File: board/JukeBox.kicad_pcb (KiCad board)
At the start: 2 copper layers, 78.5 x 80 mm, 57 parts, among them J1 USB_C_Receptacle_USB2.0, J2 Conn_01x02, J3 Conn_01x04, J4 Conn_01x03, J5 Conn_01x08, SW1 SW_SPST, SW10 SW_SPST, SW11 SW_SPST, SW12 SW_SPST, SW2 SW_SPST, SW3 SW_SPST, SW4 SW_SPST, SW5 SW_SPST, SW6 SW_SPST, SW7 SW_SPST, SW8 SW_SPST, SW9 SW_SPST, U1 ATmega8U2-A, Y1 16MHz

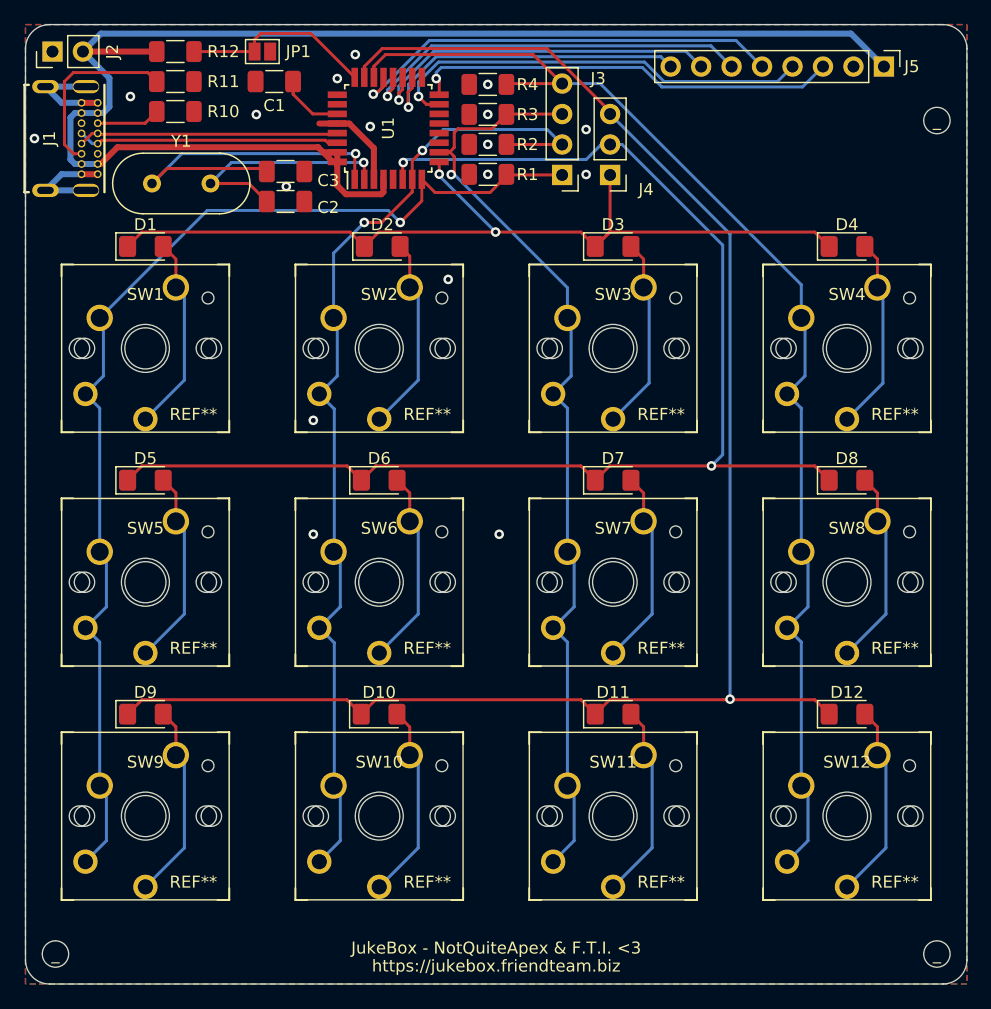
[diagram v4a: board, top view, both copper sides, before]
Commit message: fix resistors for usb in pcb
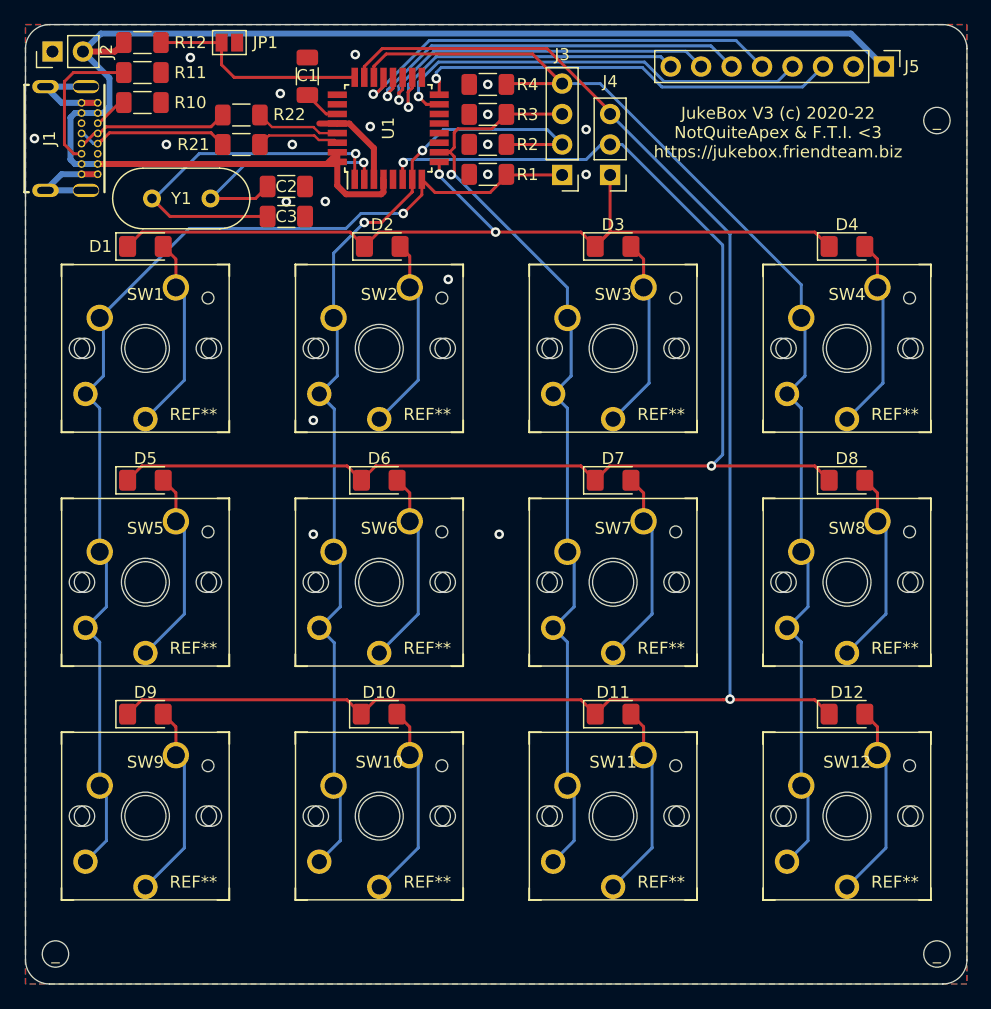
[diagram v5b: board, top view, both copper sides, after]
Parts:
- added R21: 22, Resistor_SMD:R_1206_3216Metric_Pad1.30x1.75mm_HandSolder, F.Cu at (125.0, 45.0)
- added R22: 22, Resistor_SMD:R_1206_3216Metric_Pad1.30x1.75mm_HandSolder, F.Cu at (125.0, 42.5)
- moved C3 3.75 mm to (128.8, 51.0)
- moved JP1 2.85 mm to (124.0, 36.5)
- moved R10 2.85 mm to (116.8, 41.5)
- moved R11 2.85 mm to (116.8, 39.0)
- moved R12 2.85 mm to (116.8, 36.5)
- moved C1 2.78 mm to (130.5, 39.3), turned to -90 degrees
- moved C2 1.25 mm to (128.8, 48.5)
- moved Y1 1.25 mm to (117.5, 49.5)
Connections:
- U1 pad 29: /D+ -> /D1+
- U1 pad 30: /D- -> /D1-
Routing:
- net /D+: track 21.8 -> 12.9 mm
- net /D-: track 21.1 -> 13.0 mm
- net /D1+: track 0.00 -> 7.08 mm
- net /D1-: track 0.00 -> 7.01 mm
- net Net-(J1-PadB5): track 15.5 -> 12.5 mm
- net +5V: track 120.1 -> 117.2 mm
- net Net-(J1-PadA5): track 5.33 -> 2.89 mm
- net Net-(JP1-Pad2): track 16.1 -> 18.4 mm
- net Net-(C1-Pad2): track 5.43 -> 3.15 mm
- net COL_1: track 95.4 -> 94.3 mm
- net Net-(C3-Pad2): track 30.4 -> 31.1 mm
- net GND: vias 17 -> 19
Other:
- board text added: "JukeBox V3 (c) 2020-22 NotQuiteApex & F.T.I. <3 https://jukebox.friendteam.biz"
- board text removed: "JukeBox - NotQuiteApex & F.T.I. <3"
- board text removed: "https://jukebox.friendteam.biz"

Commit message: import rp2040 minimal kicad project
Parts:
- removed D1, D10, D11, D12, D2, D3, D4, D5, D6, D7, D8, D9: DIODE, Diode_SMD:D_1206_3216Metric_Pad1.42x1.75mm_HandSolder
- removed J5: Conn_01x08, Connector_PinHeader_2.54mm:PinHeader_1x08_P2.54mm_Vertical
- removed JP1: , Jumper:SolderJumper-2_P1.3mm_Open_Pad1.0x1.5mm
- removed R10, R11: 5.11k, Resistor_SMD:R_1206_3216Metric_Pad1.30x1.75mm_HandSolder
- removed R12: 10K, Resistor_SMD:R_1206_3216Metric_Pad1.30x1.75mm_HandSolder
- removed R21, R22: 22, Resistor_SMD:R_1206_3216Metric_Pad1.30x1.75mm_HandSolder
- removed REF** (x12): SW_Cherry_MX_1.00u_PCB, Button_Switch_Keyboard:SW_Cherry_MX_1.00u_PCB
- removed SW1, SW10, SW11, SW12, SW2, SW3, SW4, SW5, SW6, SW7, SW8, SW9: SW_SPST, jukebox-footprints:Kailh_PG1350
- removed _ (x3): MountingHole_2.2mm_M2, MountingHole:MountingHole_2.2mm_M2
- added C10: 1u, Capacitor_SMD:C_0402_1005Metric, F.Cu at (104.0, 93.5)
- added C11: 100n, Capacitor_SMD:C_0402_1005Metric, F.Cu at (93.5, 97.0)
- added C12: 100n, Capacitor_SMD:C_0402_1005Metric, F.Cu at (106.5, 101.2)
- added C13: 100n, Capacitor_SMD:C_0402_1005Metric, F.Cu at (93.5, 101.2)
- added C14: 100n, Capacitor_SMD:C_0402_1005Metric, F.Cu at (100.4, 106.5)
- added C15: 100n, Capacitor_SMD:C_0402_1005Metric, F.Cu at (106.5, 96.0)
- added C16: 100n, Capacitor_SMD:C_0402_1005Metric, F.Cu at (106.5, 94.6)
- added C17: 10u, Capacitor_SMD:C_0805_2012Metric, F.Cu at (85.1, 78.0)
- added C4: 10u, Capacitor_SMD:C_0805_2012Metric, F.Cu at (109.0, 89.0)
- added C5: 100n, Capacitor_SMD:C_0402_1005Metric, F.Cu at (96.2, 82.8)
- added C6: 100n, Capacitor_SMD:C_0402_1005Metric, F.Cu at (99.0, 92.5)
- added C7: 100n, Capacitor_SMD:C_0402_1005Metric, F.Cu at (101.5, 106.5)
- added C8: 1u, Capacitor_SMD:C_0402_1005Metric, F.Cu at (103.0, 93.5)
- added C9: 100n, Capacitor_SMD:C_0402_1005Metric, F.Cu at (100.0, 92.5)
- added H1: MountingHole, MountingHole:MountingHole_2.7mm_M2.5, F.Cu at (86.0, 74.0)
- added H2: MountingHole, MountingHole:MountingHole_2.7mm_M2.5, F.Cu at (114.0, 74.0)
- added H3: MountingHole, MountingHole:MountingHole_2.7mm_M2.5, F.Cu at (114.0, 117.2)
- added H4: MountingHole, MountingHole:MountingHole_2.7mm_M2.5, F.Cu at (86.0, 117.2)
- added R5: 1k, Capacitor_SMD:C_0402_1005Metric, F.Cu at (98.7, 107.1)
- added U2: W25Q128JVS, Package_SO:SOIC-8_5.23x5.23mm_P1.27mm, F.Cu at (93.0, 87.3)
- added U3: RP2040, RP2040_minimal:RP2040-QFN-56, F.Cu at (100.0, 100.0)
- C1: value 1uF -> 10u; footprint Capacitor_SMD:C_1206_3216Metric_Pad1.33x1.80mm_HandSolder -> Capacitor_SMD:C_0805_2012Metric
- C2, C3: value 18pF -> 27p; footprint Capacitor_SMD:C_1206_3216Metric_Pad1.33x1.80mm_HandSolder -> Capacitor_SMD:C_0402_1005Metric
- J1: value USB_C_Receptacle_USB2.0 -> USB_B_Micro; footprint jukebox-footprints:GCT_USB4085-GF-A_REVA4 -> RP2040_minimal:USB_Micro-B_Amphenol_10103594-0001LF_Horizontal_modified
- J3: value Conn_01x04 -> Conn_02x18_Odd_Even; footprint Connector_PinHeader_2.54mm:PinHeader_1x04_P2.54mm_Vertical -> Connector_PinHeader_2.54mm:PinHeader_2x18_P2.54mm_Vertical
- J4: value Conn_01x03 -> Conn_02x18_Odd_Even; footprint Connector_PinHeader_2.54mm:PinHeader_1x03_P2.54mm_Vertical -> Connector_PinHeader_2.54mm:PinHeader_2x18_P2.54mm_Vertical
- R1: value 10k -> 1k; footprint Resistor_SMD:R_1206_3216Metric_Pad1.30x1.75mm_HandSolder -> Capacitor_SMD:C_0402_1005Metric
- R2: value 10k -> DNF; footprint Resistor_SMD:R_1206_3216Metric_Pad1.30x1.75mm_HandSolder -> Capacitor_SMD:C_0402_1005Metric
- R3, R4: value 10k -> 27; footprint Resistor_SMD:R_1206_3216Metric_Pad1.30x1.75mm_HandSolder -> Capacitor_SMD:C_0402_1005Metric
- U1: value ATmega8U2-A -> NCP1117-3.3_SOT223; footprint Package_QFP:TQFP-32_7x7mm_P0.8mm -> Package_TO_SOT_SMD:SOT-223-3_TabPin2
- Y1: value 16MHz -> ABLS-12.000MHZ-B4-T; footprint Crystal:Crystal_HC49-4H_Vertical -> RP2040_minimal:Crystal_SMD_HC49-US
- moved J3 80.4 mm to (75.9, 74.0), turned to 0 degrees
- moved R4 69.0 mm to (102.0, 93.5), turned to -90 degrees
- moved C2 68.6 mm to (96.5, 109.0)
- moved R3 67.7 mm to (101.0, 93.5), turned to -90 degrees
- moved R2 67.3 mm to (89.5, 82.3), turned to -90 degrees
- moved Y1 66.6 mm to (97.8, 113.1)
- moved C3 65.0 mm to (99.5, 109.0), turned to 0 degrees
- moved R1 64.7 mm to (91.0, 82.3), turned to 90 degrees
- moved U1 48.9 mm to (108.0, 82.8), turned to -90 degrees
- moved C1 43.5 mm to (107.9, 76.5), turned to 0 degrees
- moved J2 43.3 mm to (91.1, 76.5), turned to 180 degrees
- moved J4 43.2 mm to (121.6, 74.0), turned to 0 degrees
- moved J1 28.7 mm to (100.0, 71.7), turned to 180 degrees
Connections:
- C1 pad 1: GND -> VBUS
- C1 pad 2: Net-(C1-Pad2) -> GND
- C2 pad 1: GND -> /XIN
- C2 pad 2: Net-(C2-Pad2) -> GND
- C3 pad 1: GND -> Net-(C3-Pad1)
- C3 pad 2: Net-(C3-Pad2) -> GND
- J2 pad 1: GND -> /~{USB_BOOT}
- J2 pad 2: +5V -> GND
- J3 pad 1: COL_1 -> GND
- J3 pad 2: COL_2 -> +3V3
- J3 pad 3: COL_3 -> GND
- J3 pad 4: COL_4 -> /GPIO0
- J4 pad 1: ROW_1 -> /GPIO29_ADC3
- J4 pad 2: ROW_2 -> GND
- J4 pad 3: ROW_3 -> /GPIO28_ADC2
- R1 pad 1: GND -> /QSPI_SS
- R1 pad 2: COL_1 -> /~{USB_BOOT}
- R2 pad 1: GND -> +3V3
- R2 pad 2: COL_2 -> /QSPI_SS
- R3 pad 1: GND -> /USB_D+
- R3 pad 2: COL_3 -> Net-(R3-Pad2)
- R4 pad 1: GND -> /USB_D-
- R4 pad 2: COL_4 -> Net-(R4-Pad2)
- U1 pad 1: Net-(C3-Pad2) -> GND
- U1 pad 2: Net-(C2-Pad2) -> +3V3
- U1 pad 3: GND -> VBUS
- Y1 pad 1: Net-(C3-Pad2) -> /XIN
- Y1 pad 2: Net-(C2-Pad2) -> Net-(C3-Pad1)
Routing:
- net ROW_3: track 138.8 -> 0.00 mm, vias 1 -> 0
- net +5V: track 117.2 -> 0.00 mm
- net ROW_2: track 112.4 -> 0.00 mm, vias 2 -> 0
- net COL_4: track 101.4 -> 0.00 mm
- net COL_1: track 94.3 -> 0.00 mm, vias 1 -> 0
- net COL_2: track 84.4 -> 0.00 mm, vias 2 -> 0
- net COL_3: track 80.4 -> 0.00 mm, vias 1 -> 0
- net ROW_1: track 75.8 -> 0.00 mm, vias 2 -> 0
- net +3V3: track 0.00 -> 45.2 mm, vias 0 -> 2
- net CS: track 37.0 -> 0.00 mm, vias 1 -> 0
- net CLK: track 36.3 -> 0.00 mm, vias 1 -> 0
- net DIN: track 35.8 -> 0.00 mm, vias 1 -> 0
- net DC: track 33.2 -> 0.00 mm, vias 1 -> 0
- net /GPIO29_ADC3: track 0.00 -> 33.2 mm
- net /GPIO0: track 0.00 -> 31.8 mm
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- added copper zone on F.Cu, net +1V1
- added copper zone on F.Cu, net +3V3
- added copper zone on F.Cu, net VBUS
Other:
- board size 78.5 x 80 mm -> 52 x 51 mm
- rule pad_to_mask_clearance: 0 -> 0.051
- board text added: "3V3"
- board text added: "GND"
- board text added: "GP0"
- board text added: "GP1"
- board text added: "GP10"
- board text added: "GP11"
- board text added: "GP12"
- board text added: "GP13"
- board text added: "GP14"
- board text added: "GP15"
- board text added: "GP16"
- board text added: "GP17"
- board text added: "GP18"
- board text added: "GP19"
- board text added: "GP2"
- board text added: "GP20"
- board text added: "GP21"
- board text added: "GP22"
- board text added: "GP23"
- board text added: "GP24"
- board text added: "GP25"
- board text added: "GP26"
- board text added: "GP27"
- board text added: "GP28"
- board text added: "GP29"
- board text added: "GP3"
- board text added: "GP4"
- board text added: "GP5"
- board text added: "GP6"
- board text added: "GP7"
- board text added: "GP8"
- board text added: "GP9"
- board text added: "Minimal Design Example REV1"
- board text added: "Outer Row GND"
- board text added: "RUN"
- board text added: "Raspberry Pi RP2040"
- board text added: "SWCLK"
- board text added: "SWD"
- board text added: "USB_BOOT"
- board text removed: "JukeBox V3 (c) 2020-22 NotQuiteApex & F.T.I. <3 https://jukebox.friendteam.biz"

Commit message: first pass over pcb
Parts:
- removed C11, C12, C13, C14, C15, C16, C9: 100n, Capacitor_SMD:C_0402_1005Metric
- removed C17: 10u, Capacitor_SMD:C_0805_2012Metric
- removed J4: Conn_02x18_Odd_Even, Connector_PinHeader_2.54mm:PinHeader_2x18_P2.54mm_Vertical
- added D1: DIODE, Diode_SMD:D_1206_3216Metric_Pad1.42x1.75mm_HandSolder, B.Cu at (61.1, 72.5)
- added D10: DIODE, Diode_SMD:D_1206_3216Metric_Pad1.42x1.75mm_HandSolder, B.Cu at (80.6, 111.5)
- added D11: DIODE, Diode_SMD:D_1206_3216Metric_Pad1.42x1.75mm_HandSolder, B.Cu at (100.1, 111.5)
- added D12: DIODE, Diode_SMD:D_1206_3216Metric_Pad1.42x1.75mm_HandSolder, B.Cu at (119.6, 111.5)
- added D13: WS2812B, LED_SMD:LED_WS2812B_PLCC4_5.0x5.0mm_P3.2mm, F.Cu at (61.1, 70.0)
- added D14: WS2812B, LED_SMD:LED_WS2812B_PLCC4_5.0x5.0mm_P3.2mm, F.Cu at (80.6, 70.0)
- added D15: WS2812B, LED_SMD:LED_WS2812B_PLCC4_5.0x5.0mm_P3.2mm, F.Cu at (100.1, 70.0)
- added D16: WS2812B, LED_SMD:LED_WS2812B_PLCC4_5.0x5.0mm_P3.2mm, F.Cu at (119.6, 70.0)
- added D17: WS2812B, LED_SMD:LED_WS2812B_PLCC4_5.0x5.0mm_P3.2mm, F.Cu at (61.1, 89.5)
- added D18: WS2812B, LED_SMD:LED_WS2812B_PLCC4_5.0x5.0mm_P3.2mm, F.Cu at (80.6, 89.5)
- added D19: WS2812B, LED_SMD:LED_WS2812B_PLCC4_5.0x5.0mm_P3.2mm, F.Cu at (100.1, 89.5)
- added D2: DIODE, Diode_SMD:D_1206_3216Metric_Pad1.42x1.75mm_HandSolder, B.Cu at (80.6, 72.5)
- added D20: WS2812B, LED_SMD:LED_WS2812B_PLCC4_5.0x5.0mm_P3.2mm, F.Cu at (119.6, 89.5)
- added D21: WS2812B, LED_SMD:LED_WS2812B_PLCC4_5.0x5.0mm_P3.2mm, F.Cu at (61.1, 109.0)
- added D22: WS2812B, LED_SMD:LED_WS2812B_PLCC4_5.0x5.0mm_P3.2mm, F.Cu at (80.6, 109.0)
- added D23: WS2812B, LED_SMD:LED_WS2812B_PLCC4_5.0x5.0mm_P3.2mm, F.Cu at (100.1, 109.0)
- added D24: WS2812B, LED_SMD:LED_WS2812B_PLCC4_5.0x5.0mm_P3.2mm, F.Cu at (119.6, 109.0)
- added D3: DIODE, Diode_SMD:D_1206_3216Metric_Pad1.42x1.75mm_HandSolder, B.Cu at (100.1, 72.5)
- added D4: DIODE, Diode_SMD:D_1206_3216Metric_Pad1.42x1.75mm_HandSolder, B.Cu at (119.6, 72.5)
- added D5: DIODE, Diode_SMD:D_1206_3216Metric_Pad1.42x1.75mm_HandSolder, B.Cu at (61.1, 92.0)
- added D6: DIODE, Diode_SMD:D_1206_3216Metric_Pad1.42x1.75mm_HandSolder, B.Cu at (80.6, 92.0)
- added D7: DIODE, Diode_SMD:D_1206_3216Metric_Pad1.42x1.75mm_HandSolder, B.Cu at (100.1, 92.0)
- added D8: DIODE, Diode_SMD:D_1206_3216Metric_Pad1.42x1.75mm_HandSolder, B.Cu at (119.6, 92.0)
- added D9: DIODE, Diode_SMD:D_1206_3216Metric_Pad1.42x1.75mm_HandSolder, B.Cu at (61.1, 111.5)
- added JP1: SolderJumper_2_Open, Jumper:SolderJumper-2_P1.3mm_Open_RoundedPad1.0x1.5mm, F.Cu at (67.1, 67.0)
- added R11: 10k, Resistor_SMD:R_1206_3216Metric_Pad1.30x1.75mm_HandSolder, B.Cu at (86.6, 71.0)
- added R12: 10k, Resistor_SMD:R_1206_3216Metric_Pad1.30x1.75mm_HandSolder, B.Cu at (89.1, 71.0)
- added R13: 10k, Resistor_SMD:R_1206_3216Metric_Pad1.30x1.75mm_HandSolder, B.Cu at (91.6, 71.0)
- added R14: 10k, Resistor_SMD:R_1206_3216Metric_Pad1.30x1.75mm_HandSolder, B.Cu at (94.1, 71.0)
- added R6: 5.11k, Resistor_SMD:R_1206_3216Metric_Pad1.30x1.75mm_HandSolder, B.Cu at (55.1, 62.5)
- added R7: 5.11k, Resistor_SMD:R_1206_3216Metric_Pad1.30x1.75mm_HandSolder, B.Cu at (56.6, 52.5)
- added SW1: SW_SPST, RP2040_minimal:Kailh_Choc_MX_Key, F.Cu at (61.1, 79.5)
- added SW10: SW_SPST, RP2040_minimal:Kailh_Choc_MX_Key, F.Cu at (80.6, 118.5)
- added SW11: SW_SPST, RP2040_minimal:Kailh_Choc_MX_Key, F.Cu at (100.1, 118.5)
- added SW12: SW_SPST, RP2040_minimal:Kailh_Choc_MX_Key, F.Cu at (119.6, 118.5)
- added SW2: SW_SPST, RP2040_minimal:Kailh_Choc_MX_Key, F.Cu at (80.6, 79.5)
- added SW3: SW_SPST, RP2040_minimal:Kailh_Choc_MX_Key, F.Cu at (100.1, 79.5)
- added SW4: SW_SPST, RP2040_minimal:Kailh_Choc_MX_Key, F.Cu at (119.6, 79.5)
- added SW5: SW_SPST, RP2040_minimal:Kailh_Choc_MX_Key, F.Cu at (61.1, 99.0)
- added SW6: SW_SPST, RP2040_minimal:Kailh_Choc_MX_Key, F.Cu at (80.6, 99.0)
- added SW7: SW_SPST, RP2040_minimal:Kailh_Choc_MX_Key, F.Cu at (100.1, 99.0)
- added SW8: SW_SPST, RP2040_minimal:Kailh_Choc_MX_Key, F.Cu at (119.6, 99.0)
- added SW9: SW_SPST, RP2040_minimal:Kailh_Choc_MX_Key, F.Cu at (61.1, 118.5)
- C1, C4: footprint Capacitor_SMD:C_0805_2012Metric -> Capacitor_SMD:C_1206_3216Metric_Pad1.33x1.80mm_HandSolder; moved to B.Cu
- C10, C2, C3, C5, C6, C7, C8: footprint Capacitor_SMD:C_0402_1005Metric -> Capacitor_SMD:C_1206_3216Metric_Pad1.33x1.80mm_HandSolder
- J1: value USB_B_Micro -> USB_C_Receptacle_USB2.0; footprint RP2040_minimal:USB_Micro-B_Amphenol_10103594-0001LF_Horizontal_modified -> RP2040_minimal:GCT_USB4085-GF-A_REVA4
- J2: value Conn_01x02 -> Conn_01x03; footprint Connector_PinHeader_2.54mm:PinHeader_1x02_P2.54mm_Vertical -> Connector_PinHeader_2.54mm:PinHeader_1x03_P2.54mm_Vertical
- J3: value Conn_02x18_Odd_Even -> Conn_01x04; footprint Connector_PinHeader_2.54mm:PinHeader_2x18_P2.54mm_Vertical -> Connector_PinHeader_2.54mm:PinHeader_1x04_P2.54mm_Vertical
- R1, R2, R3, R4, R5: footprint Capacitor_SMD:C_0402_1005Metric -> Resistor_SMD:R_1206_3216Metric_Pad1.30x1.75mm_HandSolder
- U1: moved to B.Cu
- moved C2 88.9 mm to (99.1, 20.1), turned to 0 degrees
- moved R2 83.3 mm to (36.6, 18.0), turned to 0 degrees
- moved C7 83.1 mm to (105.1, 23.5), turned to 0 degrees
- moved C8 73.8 mm to (111.1, 20.1), turned to 0 degrees
- moved C6 65.4 mm to (116.6, 29.5), turned to 0 degrees
- moved C5 63.3 mm to (105.1, 20.1), turned to 0 degrees
- moved C3 62.6 mm to (85.6, 48.0), turned to 180 degrees
- moved Y1 58.1 mm to (114.6, 57.5), turned to 90 degrees
- moved R5 57.1 mm to (85.6, 51.5), turned to 0 degrees
- moved C1 56.5 mm to (55.1, 56.5), turned to -90 degrees
- moved C4 55.4 mm to (59.6, 64.0), turned to 180 degrees
- moved J3 54.5 mm to (86.5, 127.5), turned to 90 degrees
- moved J1 53.5 mm to (48.6, 57.0), turned to -90 degrees
- moved U1 52.9 mm to (61.6, 57.5), turned to 0 degrees
- moved C10 49.2 mm to (122.6, 48.0), turned to 0 degrees
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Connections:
- J2 pad 1: /~{USB_BOOT} -> /GPIO16
- J2 pad 2: GND -> /GPIO17
- J3 pad 1: GND -> /GPIO19
- J3 pad 2: +3V3 -> /GPIO20
- J3 pad 3: GND -> /GPIO21
- J3 pad 4: /GPIO0 -> /GPIO22
- R1 pad 1: /QSPI_SS -> /~{USB_BOOT}
- R1 pad 2: /~{USB_BOOT} -> /QSPI_SS
- U3 pad 2: /GPIO0 -> /DBGRX
- U3 pad 24: /SWCLK -> /DBGSC
- U3 pad 25: /SWD -> /DBGSD
- U3 pad 3: /GPIO1 -> /DBGTX
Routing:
- net +3V3: track 45.2 -> 206.0 mm, vias 2 -> 15
- net /GPIO19: track 20.1 -> 118.9 mm, vias 0 -> 1
- net /GPIO22: track 21.8 -> 105.9 mm, vias 0 -> 1
- net /GPIO20: track 20.8 -> 87.0 mm, vias 0 -> 1
- net Net-(D16-Pad2): track 0.00 -> 60.4 mm
- net Net-(D20-Pad2): track 0.00 -> 60.4 mm
- net /GPIO18: track 19.5 -> 79.2 mm, vias 0 -> 6
- net /GPIO16: track 21.2 -> 80.7 mm
- net /GPIO21: track 21.5 -> 71.2 mm, vias 0 -> 1
- net /GPIO17: track 19.4 -> 67.5 mm, vias 0 -> 6
- net /GPIO29_ADC3: track 33.2 -> 0.00 mm
- net GND: track 34.8 -> 2.70 mm, vias 28 -> 12
- net /GPIO0: track 31.8 -> 0.00 mm
- net /GPIO28_ADC2: track 31.6 -> 0.00 mm
- net /GPIO1: track 30.2 -> 0.00 mm
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- added copper zone on B.Cu, net +3V3
- removed copper zone on F.Cu, net +1V1
- removed copper zone on F.Cu, net +3V3
- removed copper zone on F.Cu, net VBUS
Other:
- board size 52 x 51 mm -> 88 x 88 mm
- board text removed: "3V3"
- board text removed: "GND"
- board text removed: "GP0"
- board text removed: "GP1"
- board text removed: "GP10"
- board text removed: "GP11"
- board text removed: "GP12"
- board text removed: "GP13"
- board text removed: "GP14"
- board text removed: "GP15"
- board text removed: "GP16"
- board text removed: "GP17"
- board text removed: "GP18"
- board text removed: "GP19"
- board text removed: "GP2"
- board text removed: "GP20"
- board text removed: "GP21"
- board text removed: "GP22"
- board text removed: "GP23"
- board text removed: "GP24"
- board text removed: "GP25"
- board text removed: "GP26"
- board text removed: "GP27"
- board text removed: "GP28"
- board text removed: "GP29"
- board text removed: "GP3"
- board text removed: "GP4"
- board text removed: "GP5"
- board text removed: "GP6"
- board text removed: "GP7"
- board text removed: "GP8"
- board text removed: "GP9"
- board text removed: "Minimal Design Example REV1"
- board text removed: "Outer Row GND"
- board text removed: "RUN"
- board text removed: "Raspberry Pi RP2040"
- board text removed: "SWCLK"
- board text removed: "SWD"
- board text removed: "USB_BOOT"

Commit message: second pass pcb
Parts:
- removed C6, C7: 100n, Capacitor_SMD:C_1206_3216Metric_Pad1.33x1.80mm_HandSolder
- added D25: LED, Diode_SMD:D_1206_3216Metric_Pad1.42x1.75mm_HandSolder, F.Cu at (211.1, 72.2)
- added D26: LED, Diode_SMD:D_1206_3216Metric_Pad1.42x1.75mm_HandSolder, F.Cu at (211.1, 74.5)
- added D27: LED, Diode_SMD:D_1206_3216Metric_Pad1.42x1.75mm_HandSolder, F.Cu at (211.1, 76.8)
- added D29: LED, Diode_SMD:D_1206_3216Metric_Pad1.42x1.75mm_HandSolder, F.Cu at (242.1, 75.8)
- added D30: LED, Diode_SMD:D_1206_3216Metric_Pad1.42x1.75mm_HandSolder, F.Cu at (242.1, 73.0)
- added J4: Conn_01x08, Connector_PinHeader_2.54mm:PinHeader_1x08_P2.54mm_Vertical, F.Cu at (224.7, 60.0)
- added J5: Conn_01x01, Connector_PinHeader_2.54mm:PinHeader_1x01_P2.54mm_Vertical, F.Cu at (177.1, 80.8)
- added J6: Conn_01x03, Connector_PinHeader_2.54mm:PinHeader_1x03_P2.54mm_Vertical, F.Cu at (238.3, 65.2)
- added J7: Conn_01x03, Connector_PinHeader_2.54mm:PinHeader_1x03_P2.54mm_Vertical, F.Cu at (247.1, 65.2)
- added J8: Conn_01x01, Connector_PinHeader_2.54mm:PinHeader_1x01_P2.54mm_Vertical, F.Cu at (254.8, 121.5)
- added R10: 10k, Resistor_SMD:R_1206_3216Metric_Pad1.30x1.75mm_HandSolder, B.Cu at (220.1, 137.0)
- added R16: 200, Resistor_SMD:R_1206_3216Metric_Pad1.30x1.75mm_HandSolder, F.Cu at (237.1, 75.8)
- added R17: 200, Resistor_SMD:R_1206_3216Metric_Pad1.30x1.75mm_HandSolder, F.Cu at (237.1, 73.0)
- added R8: 10k, Resistor_SMD:R_1206_3216Metric_Pad1.30x1.75mm_HandSolder, B.Cu at (180.1, 137.0)
- added R9: 10k, Resistor_SMD:R_1206_3216Metric_Pad1.30x1.75mm_HandSolder, B.Cu at (200.1, 137.0)
- R12, R13, R14: value 10k -> 200; moved to F.Cu
- moved J3 174.3 mm to (254.8, 82.2), turned to 0 degrees
- moved R11 167.1 mm to (240.1, 137.0), turned to 90 degrees
- moved C3 166.1 mm to (250.6, 66.9), turned to 90 degrees
- moved R2 165.3 mm to (192.3, 73.5)
- moved R5 162.1 mm to (246.8, 68.5)
- moved C2 160.2 mm to (250.6, 72.2), turned to -90 degrees
- moved C4 157.8 mm to (216.8, 76.8), turned to -90 degrees
- moved U3 147.3 mm to (227.1, 67.8)
- moved R4 145.2 mm to (216.8, 67.5)
- moved R3 144.9 mm to (216.8, 65.0)
- moved Y1 140.6 mm to (254.6, 70.0)
- moved U2 130.7 mm to (200.3, 73.0)
- moved R12 127.0 mm to (216.1, 72.2), turned to 180 degrees
- moved J2 126.4 mm to (254.8, 93.5)
- moved R13 124.5 mm to (216.1, 74.5), turned to 180 degrees
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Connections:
- net Net-(R3-Pad2) renamed /USB_R_D+
- net Net-(R4-Pad2) renamed /USB_R_D-
- D1 pad 1: /GPIO16 -> /GPIO9
- D10 pad 1: /GPIO18 -> /GPIO11
- D11 pad 1: /GPIO18 -> /GPIO11
- D12 pad 1: /GPIO18 -> /GPIO11
- D13 pad 4: /GPIO15 -> /GPIO2
- D2 pad 1: /GPIO16 -> /GPIO9
- D24 pad 2: unconnected-(D24-Pad2) -> /RGBDOUT
- D3 pad 1: /GPIO16 -> /GPIO9
- D4 pad 1: /GPIO16 -> /GPIO9
- D5 pad 1: /GPIO17 -> /GPIO10
- D6 pad 1: /GPIO17 -> /GPIO10
- D7 pad 1: /GPIO17 -> /GPIO10
- D8 pad 1: /GPIO17 -> /GPIO10
- D9 pad 1: /GPIO18 -> /GPIO11
- J1 pad P1: (no net) -> GND
- J1 pad P2: (no net) -> GND
- J1 pad P3: (no net) -> GND
- J1 pad P4: (no net) -> GND
- J2 pad 1: /GPIO16 -> /GPIO9
- J2 pad 2: /GPIO17 -> /GPIO10
- J2 pad 3: /GPIO18 -> /GPIO11
- J3 pad 1: /GPIO19 -> /GPIO12
- J3 pad 2: /GPIO20 -> /GPIO13
- J3 pad 3: /GPIO21 -> /GPIO14
- J3 pad 4: /GPIO22 -> /GPIO15
- R11 pad 2: /GPIO19 -> /GPIO15
- R12 pad 1: GND -> /GPIO3
- R12 pad 2: /GPIO20 -> Net-(R12-Pad2)
- R13 pad 1: GND -> /GPIO4
- R13 pad 2: /GPIO21 -> Net-(D26-Pad2)
- R14 pad 1: GND -> /GPIO5
- R14 pad 2: /GPIO22 -> Net-(D27-Pad2)
- SW1 pad 2: /GPIO19 -> /GPIO12
- SW10 pad 2: /GPIO20 -> /GPIO13
- SW11 pad 2: /GPIO21 -> /GPIO14
- SW12 pad 2: /GPIO22 -> /GPIO15
- SW2 pad 2: /GPIO20 -> /GPIO13
- SW3 pad 2: /GPIO21 -> /GPIO14
- SW4 pad 2: /GPIO22 -> /GPIO15
- SW5 pad 2: /GPIO19 -> /GPIO12
- SW6 pad 2: /GPIO20 -> /GPIO13
- SW7 pad 2: /GPIO21 -> /GPIO14
- SW8 pad 2: /GPIO22 -> /GPIO15
- SW9 pad 2: /GPIO19 -> /GPIO12
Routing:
- net /GPIO12: track 0.00 -> 162.6 mm, vias 0 -> 4
- net /GPIO13: track 0.00 -> 144.2 mm, vias 0 -> 2
- net /GPIO11: track 0.00 -> 136.1 mm, vias 0 -> 7
- net /GPIO14: track 0.00 -> 125.6 mm, vias 0 -> 2
- net /GPIO10: track 0.00 -> 120.1 mm, vias 0 -> 8
- net /GPIO19: track 118.9 -> 0.00 mm, vias 1 -> 0
- net /GPIO9: track 0.00 -> 109.1 mm, vias 0 -> 3
- net /GPIO22: track 105.9 -> 11.8 mm, vias 1 -> 0
- net /GPIO15: track 25.7 -> 107.0 mm, vias 0 -> 2
- net /GPIO16: track 80.7 -> 0.00 mm
- net /GPIO18: track 79.2 -> 0.00 mm, vias 6 -> 0
- net /GPIO20: track 87.0 -> 15.8 mm, vias 1 -> 0
- net /GPIO17: track 67.5 -> 0.00 mm, vias 6 -> 0
- net /GPIO21: track 71.2 -> 13.7 mm, vias 1 -> 0
- net /GPIO2: track 0.00 -> 56.0 mm
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- added copper zone on F.Cu, net +3V3
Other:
- board size 88 x 88 mm -> 90 x 90 mm
- board text added: "JukeBox v5.0 (c) 2020-2024 NotQuiteApex & F.T.I. <3 https://jukebox.friendteam.biz"
